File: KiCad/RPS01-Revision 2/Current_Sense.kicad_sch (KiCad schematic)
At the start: 7 parts, among them U8 INA139QPWRQ1

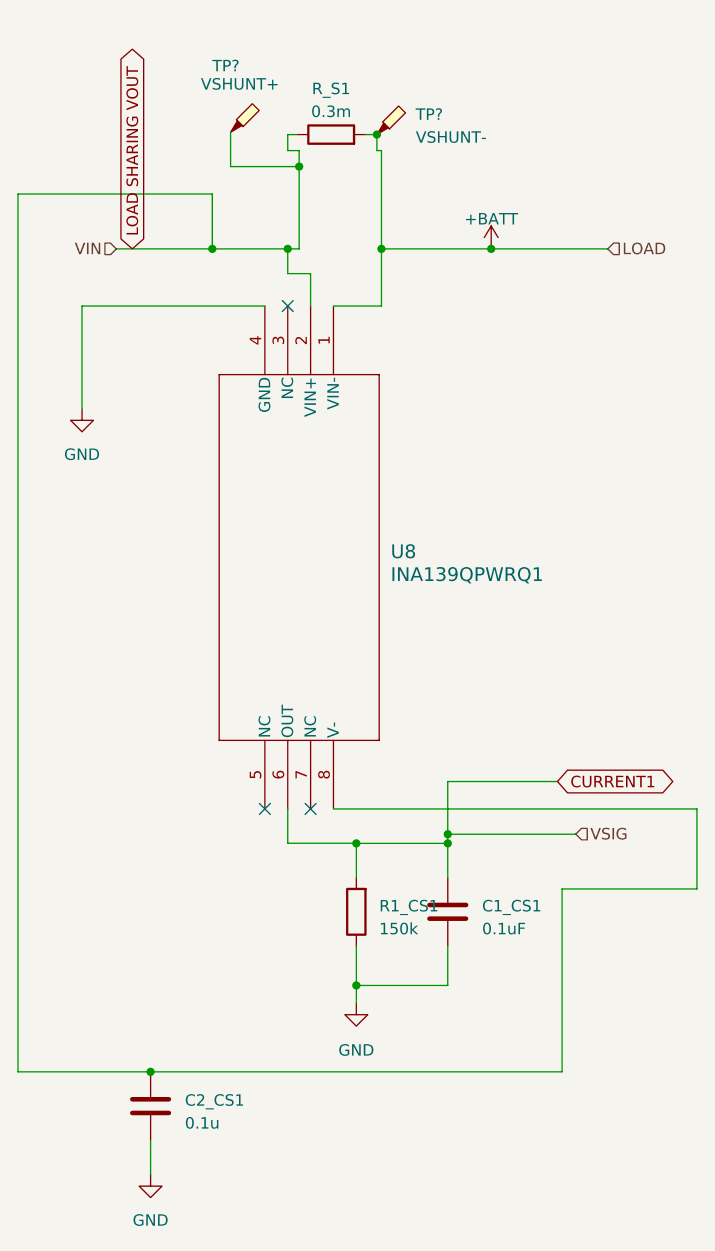
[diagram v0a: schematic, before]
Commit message: Changed Schematic Refs (pg 2 to 4)
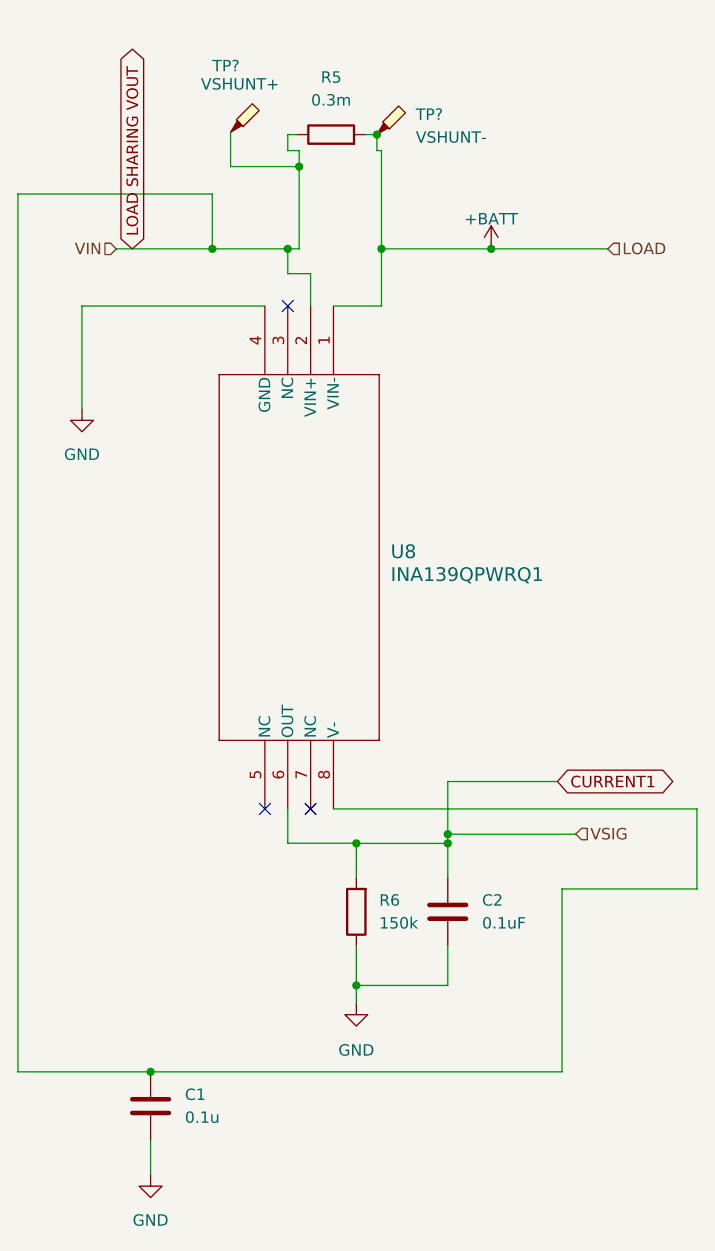
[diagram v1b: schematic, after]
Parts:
- renumbered C2_CS1 to C1, C1_CS1 to C2, R_S1 to R5, R1_CS1 to R6
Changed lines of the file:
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@@
         )
         (path "/14930f15-c0a0-4b55-93e6-b112548415f6/13e150ee-6c46-47a5-9c09-3749eb0dcbfe"
-          (reference "#PWR027") (unit 1)
+          (reference "#PWR017") (unit 1)
         )
       )
@@
         )
         (path "/14930f15-c0a0-4b55-93e6-b112548415f6/13e150ee-6c46-47a5-9c09-3749eb0dcbfe"
-          (reference "TP1") (unit 1)
+          (reference "TP2") (unit 1)
         )
       )
@@
   (symbol (lib_id "Device:R") (at 108.966 22.86 90) (unit 1)
     (in_bom yes) (on_board yes) (dnp no) (fields_autoplaced)
-    (property "Reference" "R_S1" (at 108.966 17.78 90)
-      (effects (font (size 1.27 1.27)))
-    )
-    (property "Value" "0.3m" (at 108.966 20.32 90)
+    (property "Reference" "R5" (at 108.966 16.51 90)
+      (effects (font (size 1.27 1.27)))
+    )
+    (property "Value" "0.3m" (at 108.966 19.05 90)
       (effects (font (size 1.27 1.27)))
     )
@@
       (project "rps01"
         (path "/14930f15-c0a0-4b55-93e6-b112548415f6/13e150ee-6c46-47a5-9c09-3749eb0dcbfe"
-          (reference "R_S1") (unit 1)
+          (reference "R5") (unit 1)
         )
       )
@@
   (symbol (lib_id "Device:C") (at 121.92 109.22 0) (unit 1)
     (in_bom yes) (on_board yes) (dnp no) (fields_autoplaced)
-    (property "Reference" "C1_CS1" (at 125.73 108.585 0)
-      (effects (font (size 1.27 1.27)) (justify left))
-    )
-    (property "Value" "0.1uF" (at 125.73 111.125 0)
+    (property "Reference" "C2" (at 125.73 107.95 0)
+      (effects (font (size 1.27 1.27)) (justify left))
+    )
+    (property "Value" "0.1uF" (at 125.73 110.49 0)
       (effects (font (size 1.27 1.27)) (justify left))
     )
@@
       (project "rps01"
         (path "/14930f15-c0a0-4b55-93e6-b112548415f6/13e150ee-6c46-47a5-9c09-3749eb0dcbfe"
-          (reference "C1_CS1") (unit 1)
+          (reference "C2") (unit 1)
         )
       )
@@
   (symbol (lib_id "Device:C") (at 88.9 130.81 0) (unit 1)
     (in_bom yes) (on_board yes) (dnp no) (fields_autoplaced)
-    (property "Reference" "C2_CS1" (at 92.71 130.175 0)
-      (effects (font (size 1.27 1.27)) (justify left))
-    )
-    (property "Value" "0.1u" (at 92.71 132.715 0)
+    (property "Reference" "C1" (at 92.71 129.54 0)
+      (effects (font (size 1.27 1.27)) (justify left))
+    )
+    (property "Value" "0.1u" (at 92.71 132.08 0)
       (effects (font (size 1.27 1.27)) (justify left))
     )
@@
       (project "rps01"
         (path "/14930f15-c0a0-4b55-93e6-b112548415f6/13e150ee-6c46-47a5-9c09-3749eb0dcbfe"
-          (reference "C2_CS1") (unit 1)
+          (reference "C1") (unit 1)
         )
         (path "/14930f15-c0a0-4b55-93e6-b112548415f6/83d3dc76-6aeb-422d-8708-14a32de244f0"
@@
         )
         (path "/14930f15-c0a0-4b55-93e6-b112548415f6/13e150ee-6c46-47a5-9c09-3749eb0dcbfe"
-          (reference "#PWR093") (unit 1)
+          (reference "#PWR015") (unit 1)
         )
       )
@@
   (symbol (lib_id "power:GND") (at 111.76 119.38 0) (unit 1)
     (in_bom yes) (on_board yes) (dnp no) (fields_autoplaced)
-    (property "Reference" "#PWR015" (at 111.76 125.73 0)
+    (property "Reference" "#PWR016" (at 111.76 125.73 0)
       (effects (font (size 1.27 1.27)) hide)
     )
@@
       (project "rps01"
         (path "/14930f15-c0a0-4b55-93e6-b112548415f6/13e150ee-6c46-47a5-9c09-3749eb0dcbfe"
-          (reference "#PWR015") (unit 1)
+          (reference "#PWR016") (unit 1)
         )
       )
@@
         )
         (path "/14930f15-c0a0-4b55-93e6-b112548415f6/13e150ee-6c46-47a5-9c09-3749eb0dcbfe"
-          (reference "TP2") (unit 1)
+          (reference "TP1") (unit 1)
         )
       )
@@
   (symbol (lib_id "Device:R") (at 111.76 109.22 180) (unit 1)
     (in_bom yes) (on_board yes) (dnp no) (fields_autoplaced)
-    (property "Reference" "R1_CS1" (at 114.3 108.585 0)
+    (property "Reference" "R6" (at 114.3 107.95 0)
       (effects (font (size 1.27 1.27)) (justify right))
     )
-    (property "Value" "150k" (at 114.3 111.125 0)
+    (property "Value" "150k" (at 114.3 110.49 0)
       (effects (font (size 1.27 1.27)) (justify right))
     )
@@
       (project "rps01"
         (path "/14930f15-c0a0-4b55-93e6-b112548415f6/13e150ee-6c46-47a5-9c09-3749eb0dcbfe"
-          (reference "R1_CS1") (unit 1)
-        )
-      )
+          (reference "R6") (unit 1)
+        )
+      )

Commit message: Completed Schematic
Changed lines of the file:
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@@
     )
   )
-  (hierarchical_label "LOAD" (shape input) (at 139.7 35.56 0) (fields_autoplaced)
+  (hierarchical_label "VOUT" (shape input) (at 139.7 35.56 0) (fields_autoplaced)
     (effects (font (size 1.27 1.27)) (justify left))
   )

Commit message: Finished PCB
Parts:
- removed TP?: VSHUNT-, Mechatronics TestP:CONN1_RCU-0C_TEC, symbol Connector:TestPoint_Probe
- removed TP?: VSHUNT+, Mechatronics TestP:CONN1_RCU-0C_TEC, symbol Connector:TestPoint_Probe
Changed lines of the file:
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@@
   (junction (at 114.554 35.56) (diameter 0) (color 0 0 0 0)
   )
-  (junction (at 105.41 26.416) (diameter 0) (color 0 0 0 0)
-  )
   (junction (at 126.746 35.56) (diameter 0) (color 0 0 0 0)
   )
@@
   (junction (at 121.92 100.5998) (diameter 0) (color 0 0 0 0)
   )
-  (junction (at 114.046 22.86) (diameter 0) (color 0 0 0 0)
-  )
   (junction (at 88.9 127) (diameter 0) (color 0 0 0 0)
   )
@@
     (stroke (width 0) (type default))
   )
-  (wire (pts (xy 97.79 22.606) (xy 97.79 26.416))
-    (stroke (width 0) (type default))
-  )
   (wire (pts (xy 134.62 127) (xy 88.9 127))
     (stroke (width 0) (type default))
@@
     (stroke (width 0) (type default))
   )
-  (wire (pts (xy 105.41 26.416) (xy 105.41 35.56))
+  (wire (pts (xy 105.41 24.638) (xy 105.41 35.56))
     (stroke (width 0) (type default))
   )
@@
     (stroke (width 0) (type default))
   )
-  (wire (pts (xy 97.79 26.416) (xy 105.41 26.416))
-    (stroke (width 0) (type default))
-  )
   (wire (pts (xy 114.554 35.56) (xy 126.746 35.56))
     (stroke (width 0) (type default))
@@
     (stroke (width 0) (type default))
   )
-  (wire (pts (xy 105.41 24.638) (xy 105.41 26.416))
-    (stroke (width 0) (type default))
-  )
   (wire (pts (xy 104.14 38.3106) (xy 104.14 35.56))
     (stroke (width 0) (type default))
@@
     )
   )
-  (symbol (lib_id "Connector:TestPoint_Probe") (at 114.046 22.86 0) (unit 1)
-    (in_bom yes) (on_board yes) (dnp no) (fields_autoplaced)
-    (property "Reference" "TP?" (at 118.364 20.6375 0)
-      (effects (font (size 1.27 1.27)) (justify left))
-    )
-    (property "Value" "VSHUNT-" (at 118.364 23.1775 0)
-      (effects (font (size 1.27 1.27)) (justify left))
-    )
-    (property "Footprint" "Mechatronics TestP:CONN1_RCU-0C_TEC" (at 119.126 22.86 0)
-      (effects (font (size 1.27 1.27)) hide)
-    )
-    (property "Datasheet" "~" (at 119.126 22.86 0)
-      (effects (font (size 1.27 1.27)) hide)
-    )
-    (pin "1")
-    (instances
-      (project "rps01"
-        (path "/14930f15-c0a0-4b55-93e6-b112548415f6/577d3fc4-735f-4981-a3a1-4300f23b9ae6"
-          (reference "TP?") (unit 1)
-        )
-        (path "/14930f15-c0a0-4b55-93e6-b112548415f6/13e150ee-6c46-47a5-9c09-3749eb0dcbfe"
-          (reference "TP2") (unit 1)
-        )
-      )
-    )
-  )
   (symbol (lib_id "power:GND") (at 81.28 53.34 0) (unit 1)
     (in_bom yes) (on_board yes) (dnp no) (fields_autoplaced)
@@
         )
       )
-    )
-  )
-  (symbol (lib_id "Connector:TestPoint_Probe") (at 97.79 22.606 0) (unit 1)
-    (in_bom yes) (on_board yes) (dnp no)
-    (property "Reference" "TP?" (at 95.758 15.24 0)
-      (effects (font (size 1.27 1.27)) (justify left))
-    )
-    (property "Value" "VSHUNT+" (at 94.488 17.272 0)
-      (effects (font (size 1.27 1.27)) (justify left))
-    )
-    (property "Footprint" "Mechatronics TestP:CONN1_RCU-0C_TEC" (at 102.87 22.606 0)
-      (effects (font (size 1.27 1.27)) hide)
-    )
-    (property "Datasheet" "~" (at 102.87 22.606 0)
-      (effects (font (size 1.27 1.27)) hide)
-    )
-    (pin "1")
-    (instances
-      (project "rps01"
-        (path "/14930f15-c0a0-4b55-93e6-b112548415f6/577d3fc4-735f-4981-a3a1-4300f23b9ae6"
-          (reference "TP?") (unit 1)
-        )
-        (path "/14930f15-c0a0-4b55-93e6-b112548415f6/13e150ee-6c46-47a5-9c09-3749eb0dcbfe"
-          (reference "TP1") (unit 1)
-        )
-      )

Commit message: gerbers and brendan changes
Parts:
- C2: value 0.1uF -> 0.1u
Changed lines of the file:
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@@
   (symbol (lib_id "Device:C") (at 121.92 109.22 0) (unit 1)
     (in_bom yes) (on_board yes) (dnp no) (fields_autoplaced)
-    (property "Reference" "C2" (at 125.73 107.95 0)
+    (property "Reference" "C2" (at 125.73 108.585 0)
       (effects (font (size 1.27 1.27)) (justify left))
     )
-    (property "Value" "0.1uF" (at 125.73 110.49 0)
+    (property "Value" "0.1u" (at 125.73 111.125 0)
       (effects (font (size 1.27 1.27)) (justify left))
     )
